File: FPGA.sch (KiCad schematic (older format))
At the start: 9 parts, among them U34 PCA9555AHF, U39 PCA9555AHF

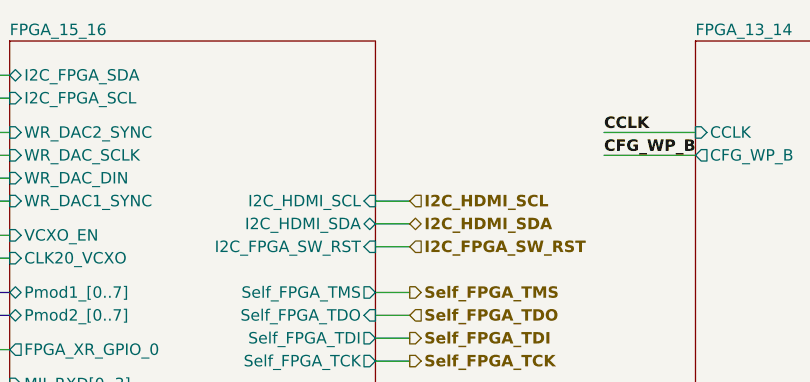
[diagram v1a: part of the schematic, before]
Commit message: less traces under SFP cage, MLVDS transceiver added, TCLKA connected to FPGA
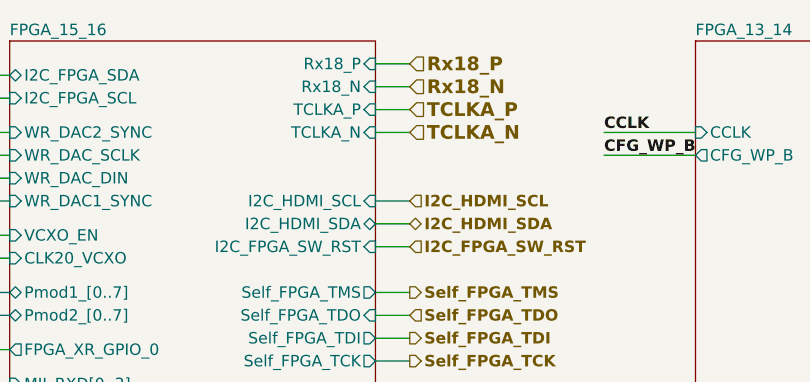
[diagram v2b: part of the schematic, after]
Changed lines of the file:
@@
 F31 "MII_RX_CLK" I L 6950 3700 50
 F32 "PHY_RSTn" I L 6950 3800 50
+F33 "TCLKA_P" I R 8550 2000 50
+F34 "TCLKA_N" I R 8550 2100 50
+F35 "Rx18_P" I R 8550 1800 50
+F36 "Rx18_N" I R 8550 1900 50
 $EndSheet
 $Sheet
@@
 NoConn ~ 8500 9850
 NoConn ~ 8500 9950
+Text HLabel 8700 2000 2    60   Input ~ 12
+TCLKA_P
+Text HLabel 8700 2100 2    60   Input ~ 12
+TCLKA_N
+Wire Wire Line
+	8550 2000 8700 2000
+Wire Wire Line
+	8550 2100 8700 2100
+Text HLabel 8700 1800 2    60   Input ~ 12
+Rx18_P
+Text HLabel 8700 1900 2    60   Input ~ 12
+Rx18_N
+Wire Wire Line
+	8700 1800 8550 1800
+Wire Wire Line
+	8700 1900 8550 1900
 $EndSCHEMATC

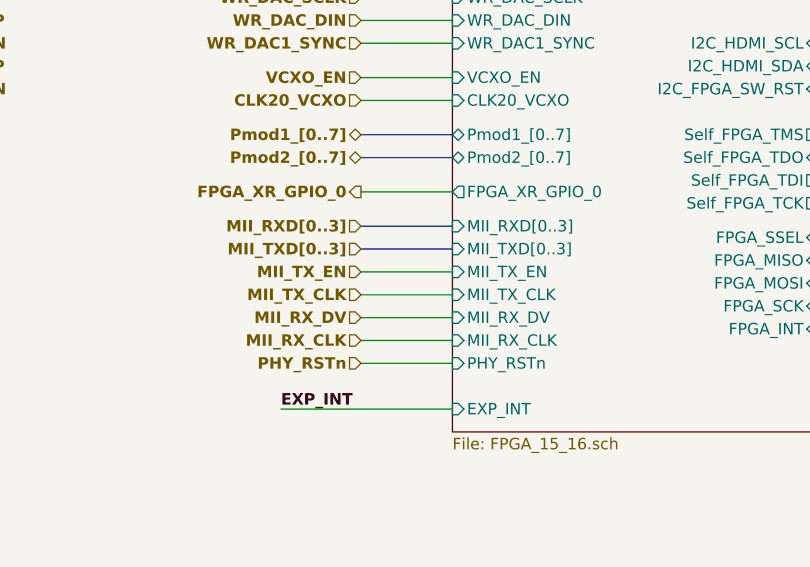
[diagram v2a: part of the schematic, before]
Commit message: U.FL for clock, logos moved, MII -> RGMII, new symbol library, git tag added
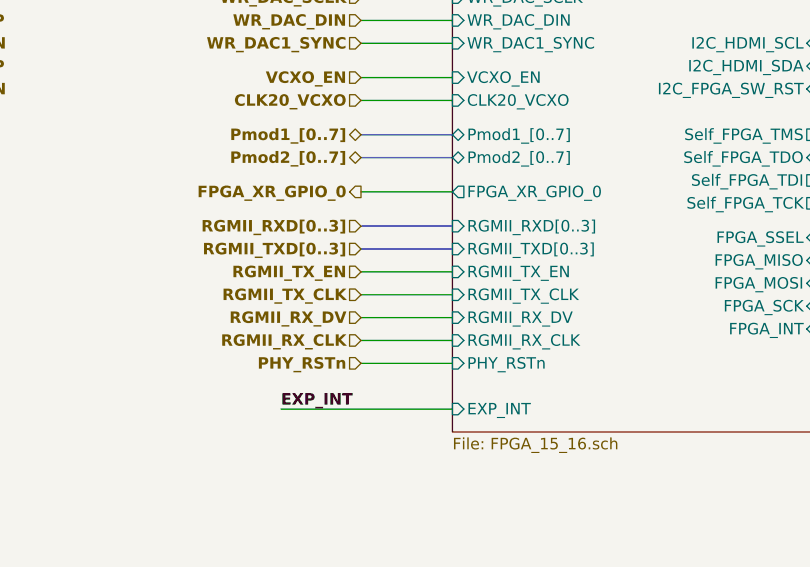
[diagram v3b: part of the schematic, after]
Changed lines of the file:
@@
 $Descr A3 16535 11693
 encoding utf-8
-Sheet 18 25
+Sheet 17 25
 Title "Marble"
 Date "2019-01-16"
@@
 F24 "I2C_HDMI_SCL" I R 8550 2400 50
 F25 "I2C_HDMI_SDA" B R 8550 2500 50
-F26 "MII_RXD[0..3]" I L 6950 3200 50
-F27 "MII_TXD[0..3]" I L 6950 3300 50
-F28 "MII_TX_EN" I L 6950 3400 50
-F29 "MII_TX_CLK" I L 6950 3500 50
-F30 "MII_RX_DV" I L 6950 3600 50
-F31 "MII_RX_CLK" I L 6950 3700 50
-F32 "PHY_RSTn" I L 6950 3800 50
-F33 "TCLKA_P" I R 8550 2000 50
-F34 "TCLKA_N" I R 8550 2100 50
-F35 "Rx18_P" I R 8550 1800 50
-F36 "Rx18_N" I R 8550 1900 50
+F26 "PHY_RSTn" I L 6950 3800 50
+F27 "TCLKA_P" I R 8550 2000 50
+F28 "TCLKA_N" I R 8550 2100 50
+F29 "Rx18_P" I R 8550 1800 50
+F30 "Rx18_N" I R 8550 1900 50
+F31 "RGMII_RXD[0..3]" I L 6950 3200 50
+F32 "RGMII_TXD[0..3]" I L 6950 3300 50
+F33 "RGMII_TX_EN" I L 6950 3400 50
+F34 "RGMII_TX_CLK" I L 6950 3500 50
+F35 "RGMII_RX_DV" I L 6950 3600 50
+F36 "RGMII_RX_CLK" I L 6950 3700 50
 $EndSheet
 $Sheet
@@
 FPGA_XR_GPIO_0
 Text HLabel 6550 3200 0    50   Input ~ 10
-MII_RXD[0..3]
+RGMII_RXD[0..3]
 Text HLabel 6550 3300 0    50   Input ~ 10
-MII_TXD[0..3]
+RGMII_TXD[0..3]
 Text HLabel 6550 3400 0    50   Input ~ 10
-MII_TX_EN
+RGMII_TX_EN
 Text HLabel 6550 3500 0    50   Input ~ 10
-MII_TX_CLK
+RGMII_TX_CLK
 Text HLabel 6550 3600 0    50   Input ~ 10
-MII_RX_DV
+RGMII_RX_DV
 Text HLabel 6550 3700 0    50   Input ~ 10
-MII_RX_CLK
+RGMII_RX_CLK
 Text HLabel 6550 3800 0    50   Input ~ 10
 PHY_RSTn

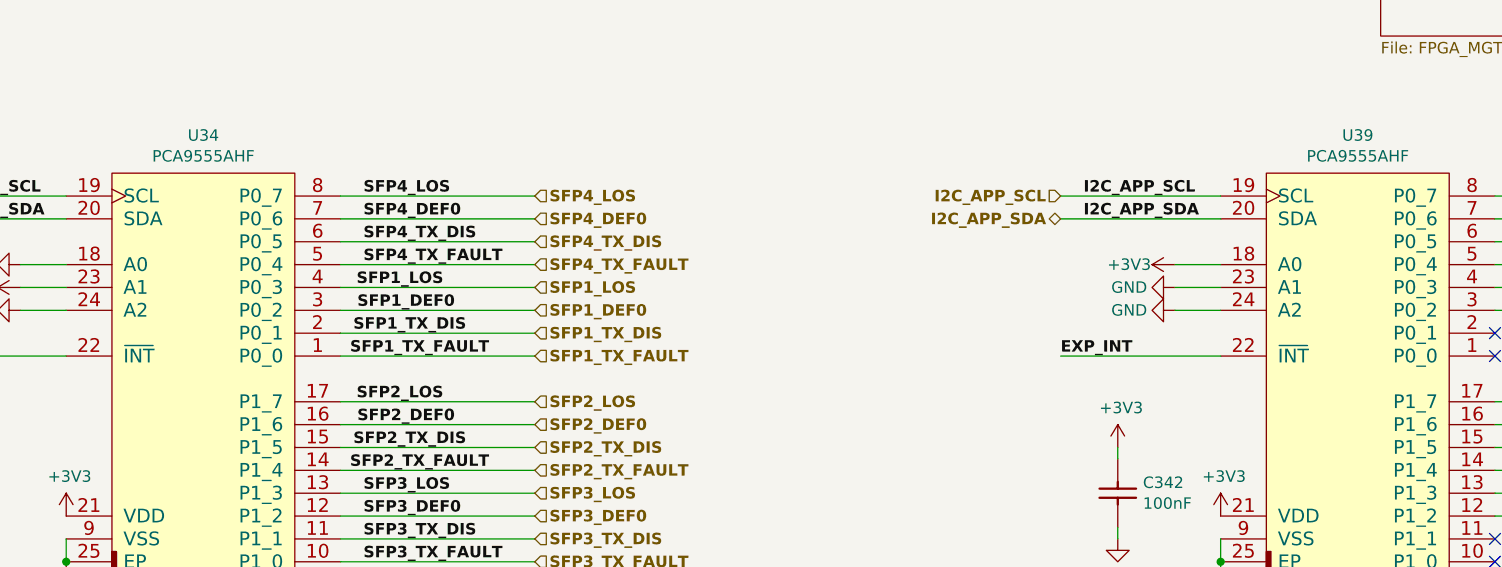
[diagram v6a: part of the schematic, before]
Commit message: SCH: Add 3rd INA219, remove +12VS power symbol
... also add some notes about current flow
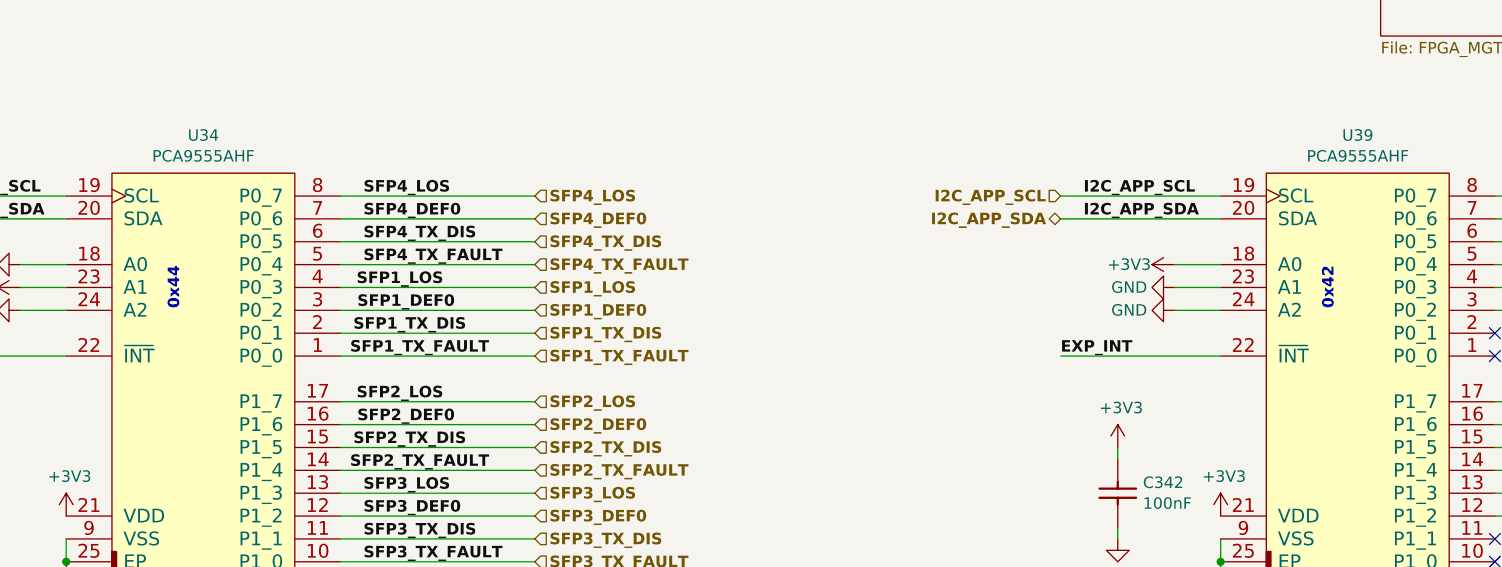
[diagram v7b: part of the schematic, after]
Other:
- note added: "0x42"
- note added: "0x44"
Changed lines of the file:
@@
 Wire Wire Line
 	8700 1900 8550 1900
+Text Notes 7800 8850 1    50   ~ 10
+0x42
+Text Notes 2750 8850 1    50   ~ 10
+0x44
 $EndSCHEMATC

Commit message: Convert all footprints to use Marble nickname
Includes both .sch and .lib files
Includes both bare footprint names and those with CERN-like nicknames
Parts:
- C215, C342: footprint CAPC0603X33N -> Marble:CAPC0603X33N
- LD11, LD12: footprint ICs And Semiconductors SMD:LED_AVAGO_HSMC-C120 -> Marble:LED_AVAGO_HSMC-C120
- R199, R264, R265: footprint RESC1005X40N -> Marble:RESC1005X40N
- U34, U39: footprint ICs And Semiconductors SMD:QFN50P400X400X80-25N-S225 -> Marble:QFN50P400X400X80-25N-S225
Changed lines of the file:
@@
 F 0 "U39" H 7900 8415 50  0000 C CNN
 F 1 "PCA9555AHF" H 7900 8324 50  0000 C CNN
-F 2 "ICs And Semiconductors SMD:QFN50P400X400X80-25N-S225" H 7500 5360 60  0001 L CNN
+F 2 "Marble:QFN50P400X400X80-25N-S225" H 7500 5360 60  0001 L CNN
 F 3 "" H 7500 6080 60  0001 L CNN
 F 4 "PCA9555AHF" H 7500 5990 60  0001 L CNN "Part Number"
@@
 F 0 "U34" H 2850 8415 50  0000 C CNN
 F 1 "PCA9555AHF" H 2850 8324 50  0000 C CNN
-F 2 "ICs And Semiconductors SMD:QFN50P400X400X80-25N-S225" H 2450 5360 60  0001 L CNN
+F 2 "Marble:QFN50P400X400X80-25N-S225" H 2450 5360 60  0001 L CNN
 F 3 "" H 2450 6080 60  0001 L CNN
 F 4 "PCA9555AHF" H 2450 5990 60  0001 L CNN "Part Number"
@@
 F 0 "C215" V 1504 9660 50  0000 L CNN
 F 1 "CC0201_100NF_6.3V_10%_X5R" H 1400 9290 60  0001 L CNN
-F 2 "CAPC0603X33N" H 1400 8480 60  0001 L CNN
+F 2 "Marble:CAPC0603X33N" H 1400 8480 60  0001 L CNN
 F 3 "\\\\cern.ch\\dfs\\Applications\\Altium\\Datasheets\\CC0201_X5R_AVX.pdf" H 1400 9110 60  0001 L CNN
 F 4 "100nF" V 1595 9660 50  0000 L CNN "~"
@@
 F 0 "C342" V 6954 9610 50  0000 L CNN
 F 1 "CC0201_100NF_6.3V_10%_X5R" H 6850 9240 60  0001 L CNN
-F 2 "CAPC0603X33N" H 6850 8430 60  0001 L CNN
+F 2 "Marble:CAPC0603X33N" H 6850 8430 60  0001 L CNN
 F 3 "\\\\cern.ch\\dfs\\Applications\\Altium\\Datasheets\\CC0201_X5R_AVX.pdf" H 6850 9060 60  0001 L CNN
 F 4 "100nF" V 7045 9610 50  0000 L CNN "~"
@@
 F 0 "R199" H 1200 8500 50  0000 L CNN
 F 1 "R0402_2K2_1%_0.0625W_100PPM" H 1100 8190 60  0001 L CNN
-F 2 "RESC1005X40N" H 1100 7380 60  0001 L CNN
+F 2 "Marble:RESC1005X40N" H 1100 7380 60  0001 L CNN
 F 3 "\\\\cern.ch\\dfs\\Applications\\Altium\\Datasheets\\R0402_Phycomp_RC0402.pdf" H 1100 8010 60  0001 L CNN
 F 4 "2k2" V 1400 8400 50  0000 L CNN "~"
@@
 F 0 "LD11" H 9850 9300 50  0000 C CNN
 F 1 "LED_AVAGO_HSMC-C120" H 9850 9170 60  0001 L CNN
-F 2 "ICs And Semiconductors SMD:LED_AVAGO_HSMC-C120" H 9850 8180 60  0001 L CNN
+F 2 "Marble:LED_AVAGO_HSMC-C120" H 9850 8180 60  0001 L CNN
 F 3 "" H 9850 8990 60  0001 L CNN
 F 4 "Red" H 9850 8900 60  0001 L CNN "Pole4"
@@
 F 0 "LD12" H 10200 9300 50  0000 C CNN
 F 1 "LED_AVAGO_HSMC-C120" H 10200 9170 60  0001 L CNN
-F 2 "ICs And Semiconductors SMD:LED_AVAGO_HSMC-C120" H 10200 8180 60  0001 L CNN
+F 2 "Marble:LED_AVAGO_HSMC-C120" H 10200 8180 60  0001 L CNN
 F 3 "" H 10200 8990 60  0001 L CNN
 F 4 "Red" H 10200 8900 60  0001 L CNN "Pole4"
@@
 F 0 "R265" V 10304 9010 50  0000 L CNN
 F 1 "R0402_1K_1%_0.0625W_100PPM" H 10200 8740 60  0001 L CNN
-F 2 "RESC1005X40N" H 10200 7930 60  0001 L CNN
+F 2 "Marble:RESC1005X40N" H 10200 7930 60  0001 L CNN
 F 3 "\\\\cern.ch\\dfs\\Applications\\Altium\\Datasheets\\R0402_Phycomp_RC0402.pdf" H 10200 8560 60  0001 L CNN
 F 4 "1k" V 10395 9010 50  0000 L CNN "~"
@@
 F 0 "R264" V 9954 9010 50  0000 L CNN
 F 1 "R0402_1K_1%_0.0625W_100PPM" H 9850 8740 60  0001 L CNN
-F 2 "RESC1005X40N" H 9850 7930 60  0001 L CNN
+F 2 "Marble:RESC1005X40N" H 9850 7930 60  0001 L CNN
 F 3 "\\\\cern.ch\\dfs\\Applications\\Altium\\Datasheets\\R0402_Phycomp_RC0402.pdf" H 9850 8560 60  0001 L CNN
 F 4 "1k" V 10045 9010 50  0000 L CNN "~"
